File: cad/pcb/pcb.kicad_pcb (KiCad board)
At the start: 4 copper layers, 104 parts, among them X1 USB_C_Receptacle_USB2.0, X2 Bat-Conn, X3 NTC-Conn, X4 SWD-Conn, X5 UART_Conn, Y1 32MHz, Y2 32.768k

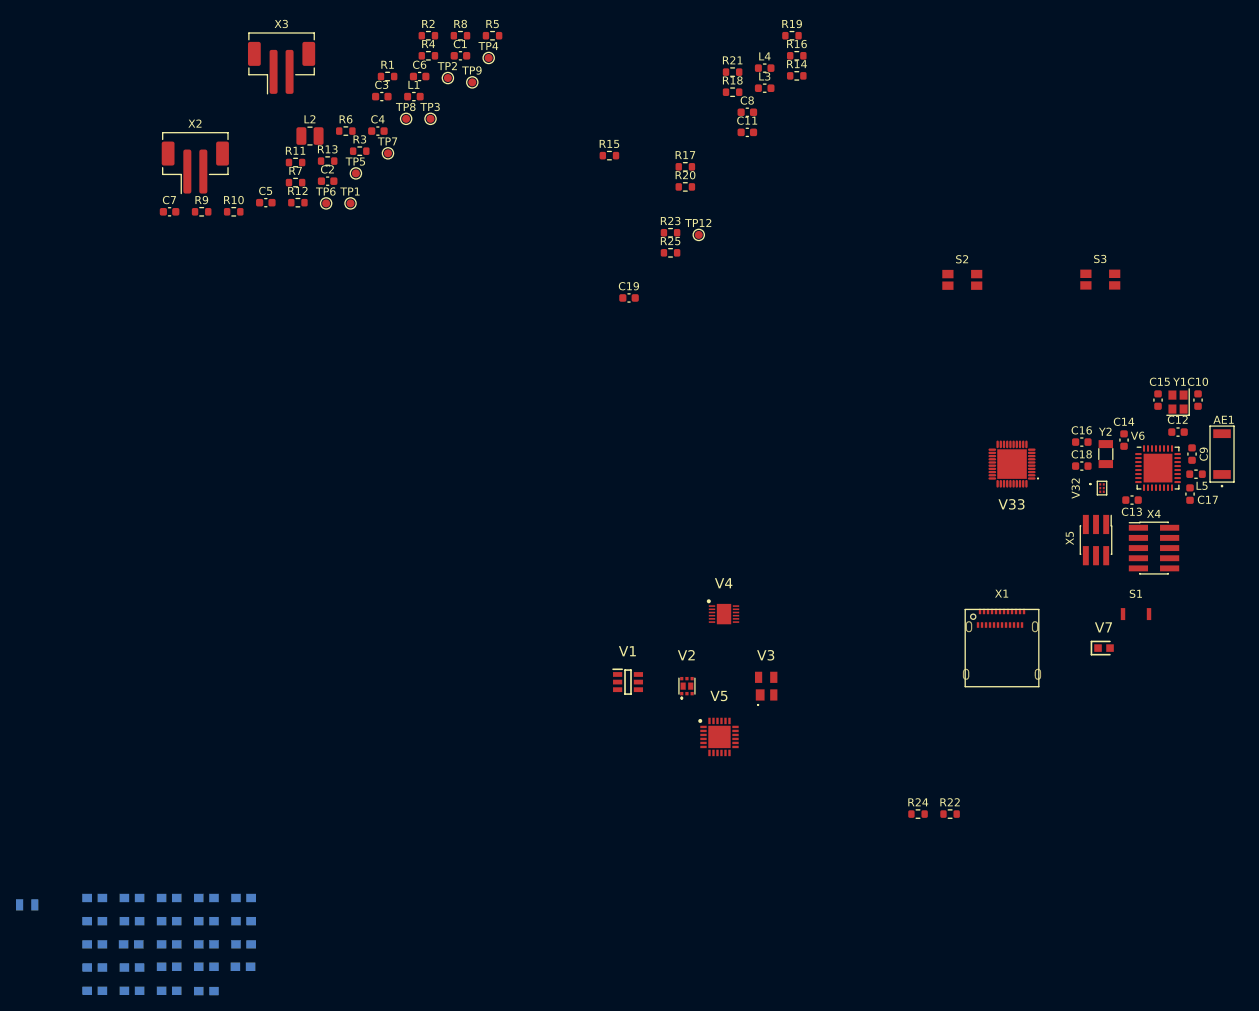
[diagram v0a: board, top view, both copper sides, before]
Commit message: finish mcu section in pcb layout
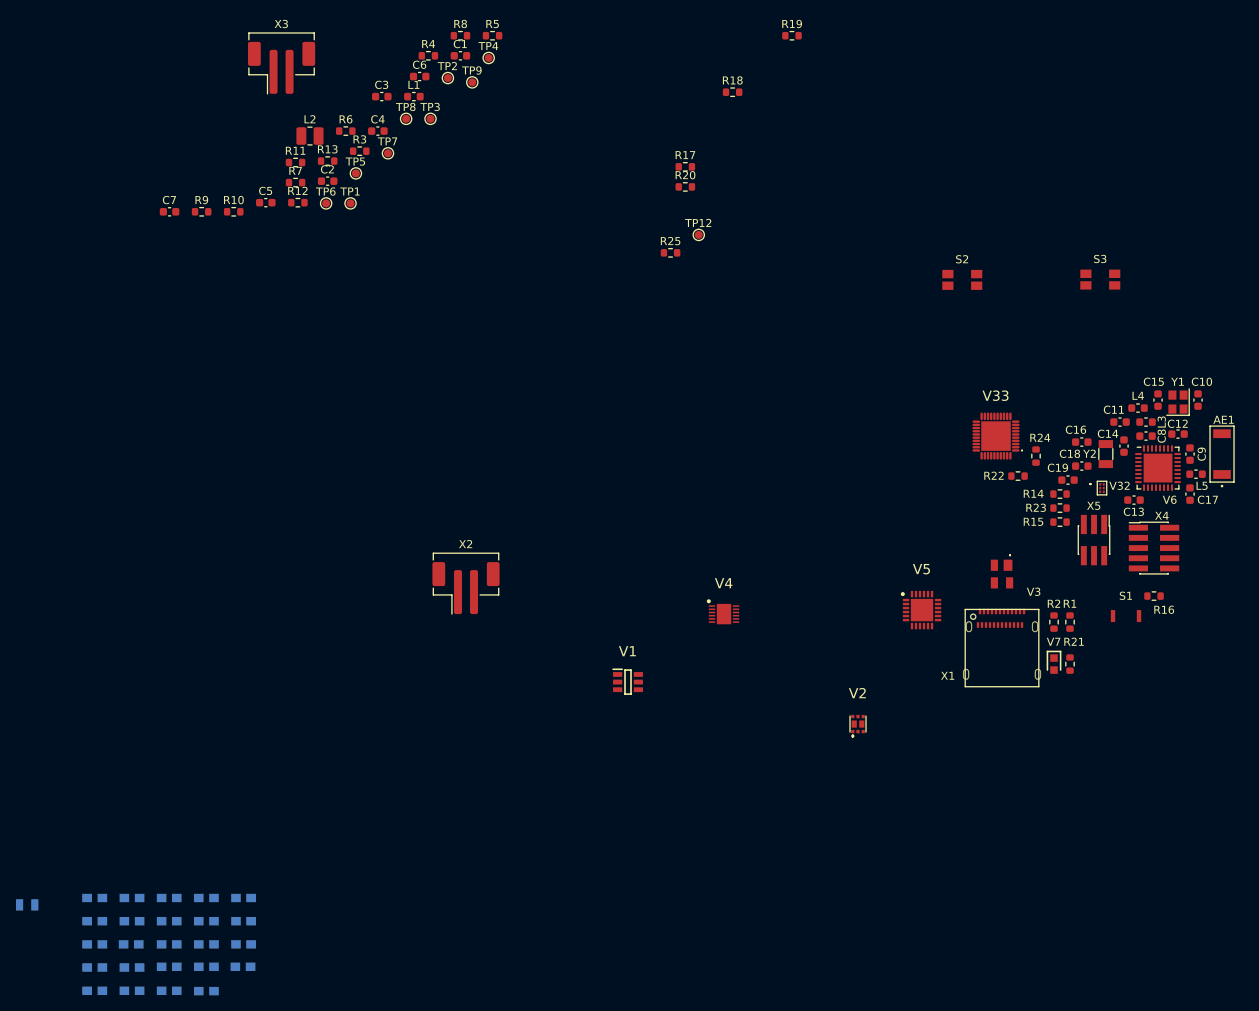
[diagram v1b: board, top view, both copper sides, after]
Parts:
- moved R1 109.2 mm to (158.5, 120.8), turned to 90 degrees
- moved R2 107.2 mm to (156.5, 120.8), turned to 90 degrees
- moved R21 85.2 mm to (158.5, 126.0), turned to -90 degrees
- moved R16 81.0 mm to (169.0, 117.5), turned to 180 degrees
- moved R15 72.6 mm to (157.2, 108.2)
- moved C8 64.2 mm to (168.0, 97.5), turned to 180 degrees
- moved L3 63.4 mm to (168.0, 95.8)
- moved L4 63.1 mm to (167.0, 94.0), turned to 180 degrees
- moved X2 62.5 mm to (83.0, 116.5)
- moved R14 61.8 mm to (157.2, 104.8)
- moved R23 59.6 mm to (157.2, 106.5)
- moved C19 59.4 mm to (158.2, 103.0), turned to 180 degrees
- moved C11 59.0 mm to (164.8, 95.8), turned to 180 degrees
- moved R24 47.1 mm to (154.2, 100.0), turned to -90 degrees
- moved R22 43.1 mm to (152.0, 102.5), turned to 180 degrees
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
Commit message: add power section on pcb layout
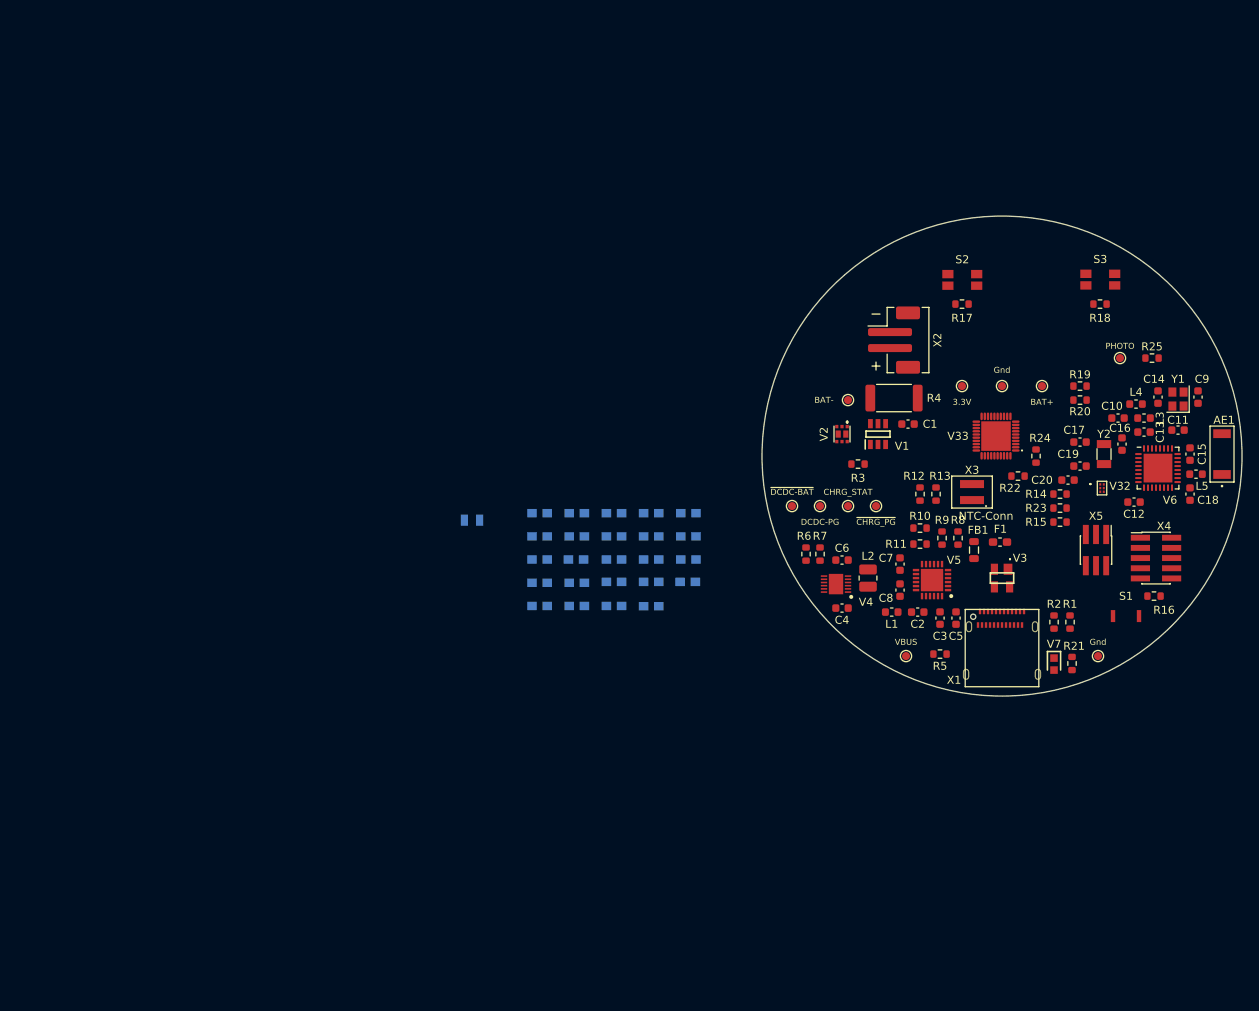
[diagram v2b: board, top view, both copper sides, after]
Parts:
- added C5: 1u, Capacitor_SMD:C_0603_1608Metric, F.Cu at (144.2, 120.2)
- added F1: Fuse_1A, Fuse:Fuse_0603_1608Metric_Pad1.05x0.95mm_HandSolder, F.Cu at (149.8, 110.8)
- added FB1: FerriteBead_Small, Inductor_SMD:L_0805_2012Metric, F.Cu at (146.5, 111.8)
- added TP6: Gnd, TestPoint:TestPoint_Pad_D1.0mm, F.Cu at (162.0, 125.0)
- R4: footprint Resistor_SMD:R_0603_1608Metric -> Resistor_SMD:R_2512_6332Metric
- X3: footprint Connector_JST:JST_PH_B2B-PH-SM4-TB_1x02-1MP_P2.00mm_Vertical -> myLib:PinHeader_P2mm_1x02_SMD
- moved C8 102.8 mm to (137.2, 116.8), turned to -90 degrees
- moved X3 101.3 mm to (146.2, 104.5), turned to 90 degrees
- moved R9 101.1 mm to (142.5, 110.2), turned to -90 degrees
- moved C3 95.5 mm to (142.2, 120.2), turned to -90 degrees
- moved R5 95.4 mm to (142.2, 124.8), turned to 180 degrees
- moved R10 94.5 mm to (139.8, 109.0)
- moved TP5 91.5 mm to (138.0, 125.0)
- moved R11 91.5 mm to (139.8, 111.0)
- moved C2 91.3 mm to (139.5, 119.5), turned to 180 degrees
- moved L2 89.0 mm to (133.2, 115.2), turned to 90 degrees
- moved R8 88.4 mm to (144.5, 110.2), turned to -90 degrees
- moved L1 87.9 mm to (136.2, 119.5), turned to 180 degrees
- moved R13 86.7 mm to (141.8, 104.8), turned to 90 degrees
- moved R12 85.9 mm to (139.8, 104.8), turned to -90 degrees
- moved C7 85.6 mm to (137.2, 113.5), turned to 90 degrees
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- renumbered C11 to C10, C12 to C11, C13 to C12, C8 to C13, C15 to C14, C9 to C15, C14 to C16, C16 to C17, C17 to C18, C18 to C19, C19 to C20, C5 to C6, C6 to C7, C7 to C8, C10 to C9, TP9 to TP10, TP12 to TP11, TP6 to TP7, TP7 to TP8, TP8 to TP9
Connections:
- V3 pad 1: VBUS -> VBUS_CONN
- X1 pad A4: VBUS -> VBUS_CONN
- X1 pad A9: VBUS -> VBUS_CONN
- X1 pad B4: VBUS -> VBUS_CONN
- X1 pad B9: VBUS -> VBUS_CONN
- X2 pad 1: BAT_PROT+ -> BAT-
- X2 pad 2: BAT- -> BAT_PROT+
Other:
- board outline added: 60 x 60 mm

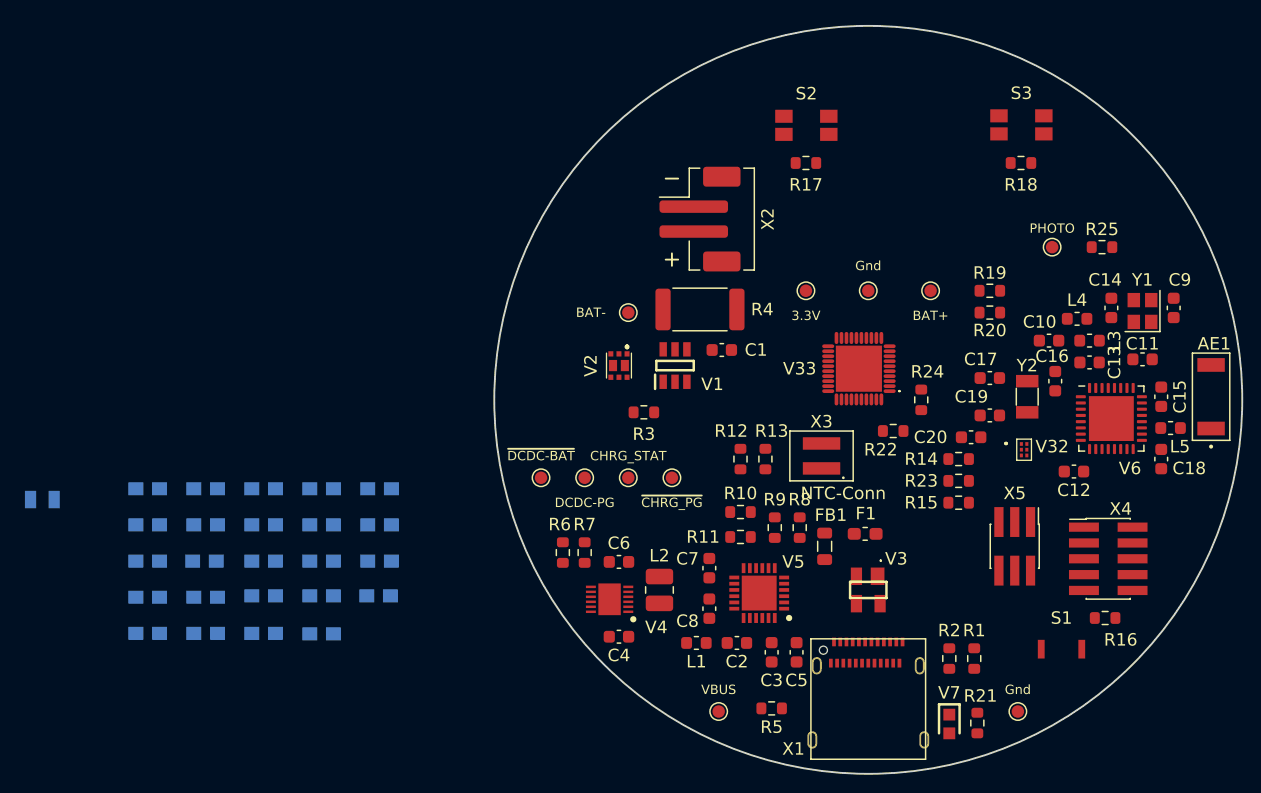
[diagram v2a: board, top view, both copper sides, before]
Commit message: add back layer led-ring
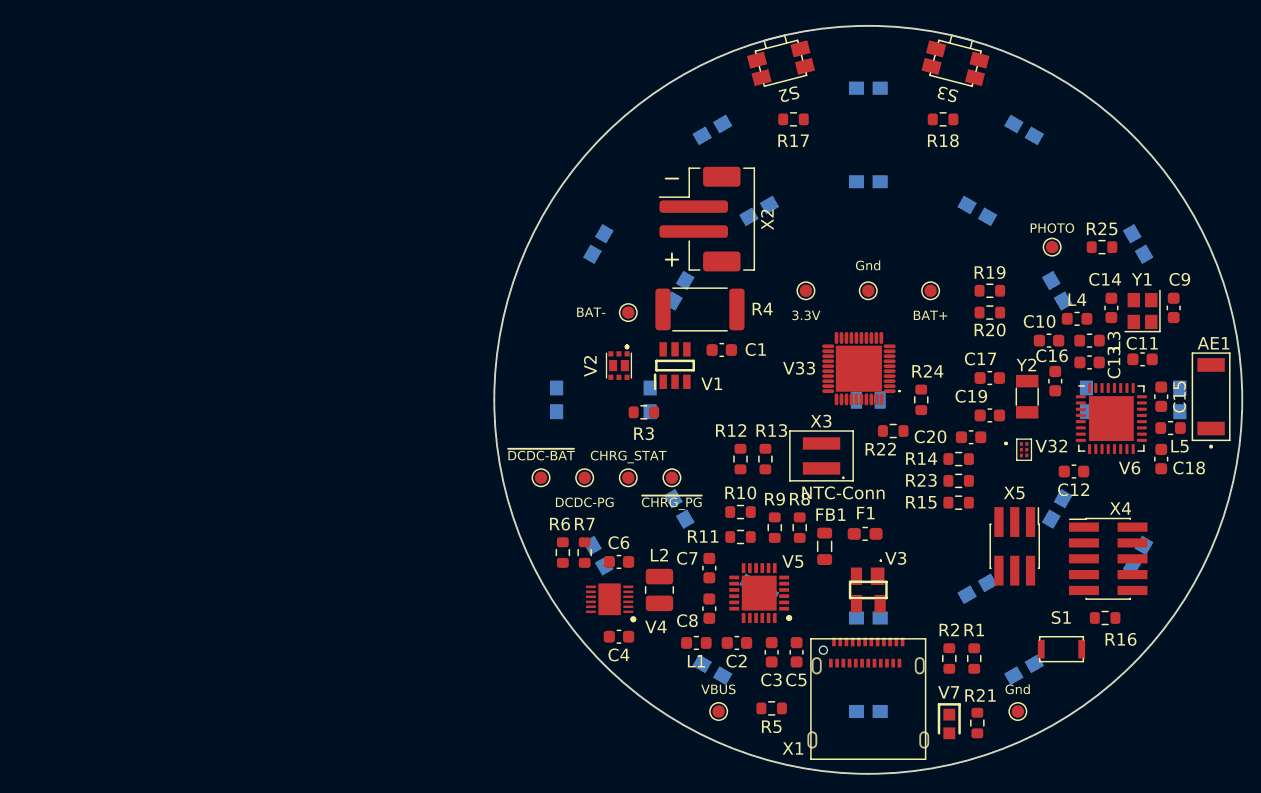
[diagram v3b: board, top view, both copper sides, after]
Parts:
- S2, S3: footprint myLib:Tactile_Panasonic_EVQ-P7J01P -> myLib:Tactile_Panasonic_EVQP7J01P
- moved V18 81.1 mm to (171.7, 87.5), turned to -60 degrees
- moved V16 79.5 mm to (171.7, 112.5), turned to -120 degrees
- moved V19 76.0 mm to (162.5, 78.3), turned to -30 degrees
- moved V29 71.0 mm to (167.5, 100.0), turned to -90 degrees
- moved V17 69.2 mm to (175.0, 100.0), turned to -90 degrees
- moved V34 66.7 mm to (150.0, 100.0), turned to 0 degrees
- moved V30 66.4 mm to (165.2, 91.2), turned to -60 degrees
- moved V20 65.3 mm to (150.0, 82.5), turned to 0 degrees
- moved V31 63.8 mm to (158.8, 84.8), turned to -30 degrees
- moved V8 63.7 mm to (150.0, 75.0), turned to 0 degrees
- moved V28 59.0 mm to (165.2, 108.8), turned to -120 degrees
- moved V27 57.4 mm to (158.8, 115.2), turned to -150 degrees
- moved V21 52.6 mm to (141.2, 84.8), turned to 30 degrees
- moved V15 52.4 mm to (162.5, 121.7), turned to -150 degrees
- moved V9 51.9 mm to (137.5, 78.3), turned to 30 degrees
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
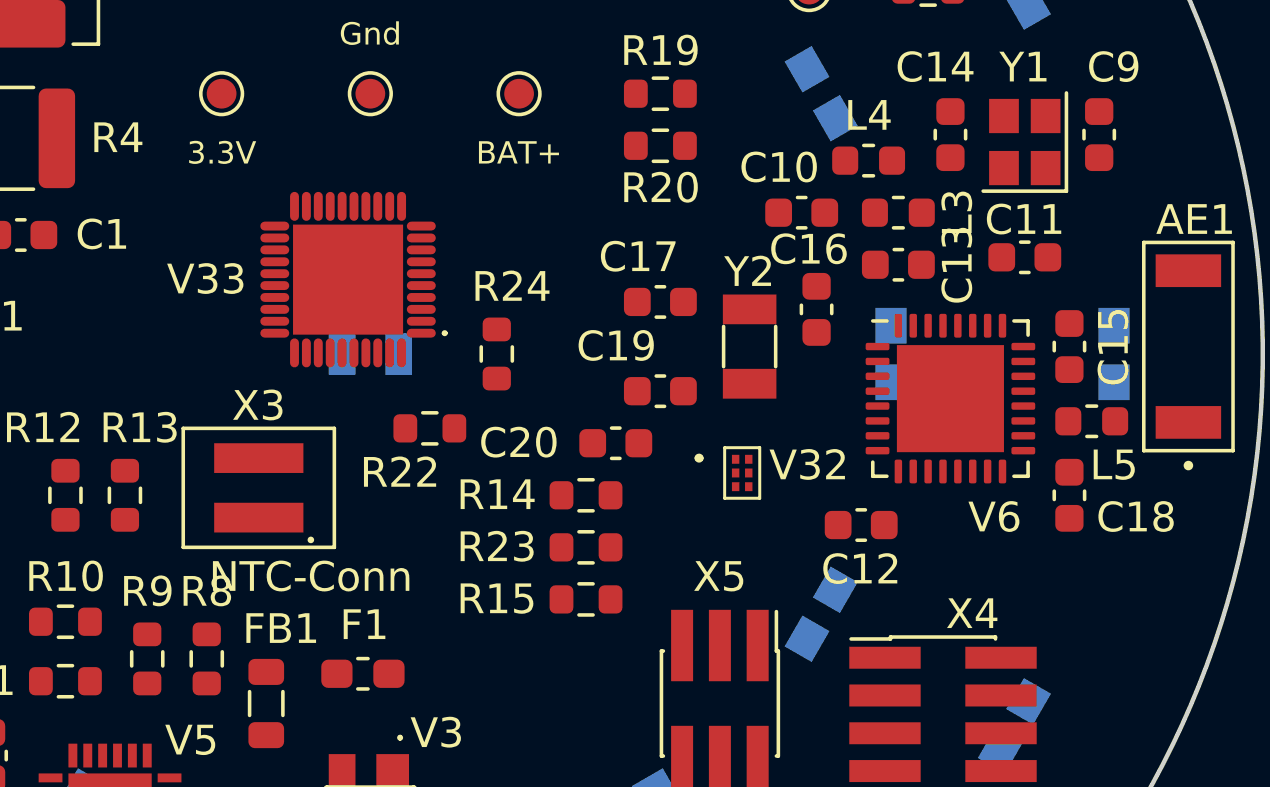
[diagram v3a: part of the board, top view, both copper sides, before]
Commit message: finish back layer placement
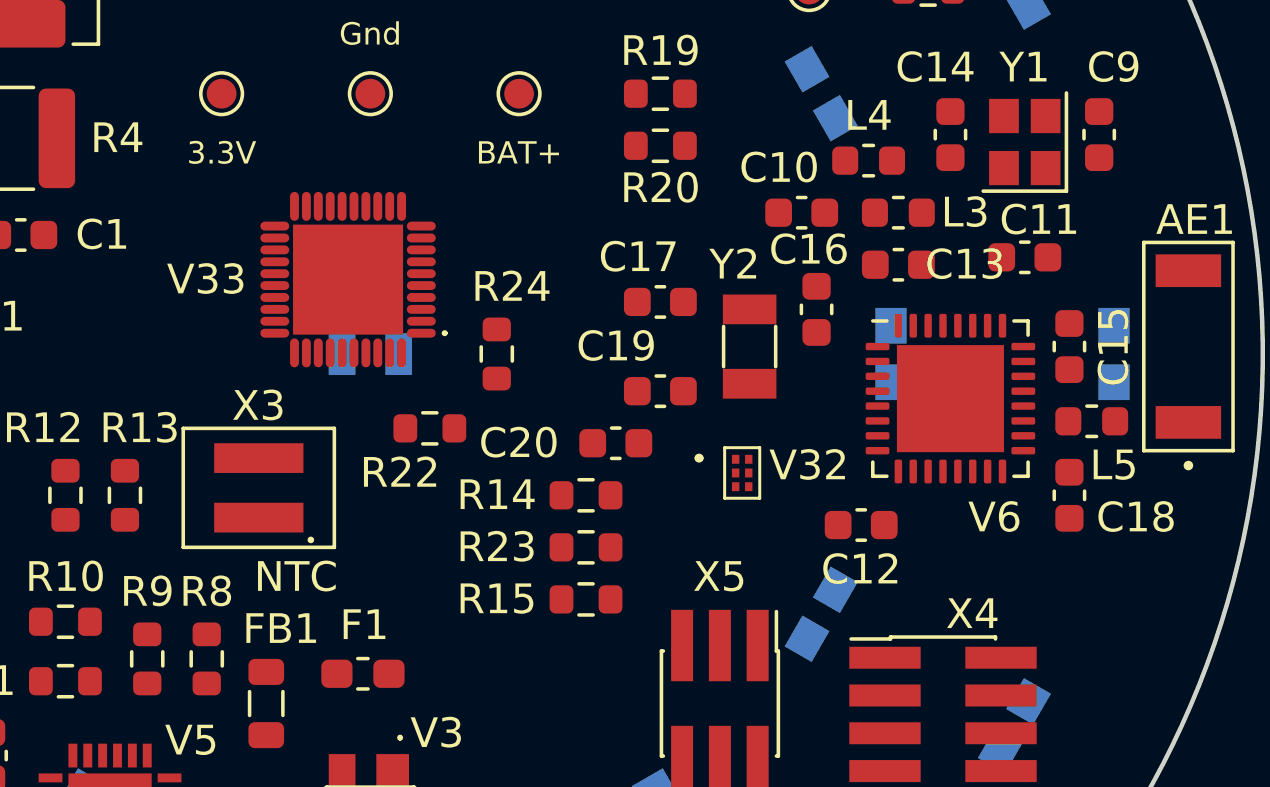
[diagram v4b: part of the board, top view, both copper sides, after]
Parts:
- X3: value NTC-Conn -> NTC
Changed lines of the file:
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@@
     (property "Sheetname" "MCU")
     (attr smd)
-    (fp_text reference "Y2" (at -2.5 0 180) (layer "F.SilkS")
+    (fp_text reference "Y2" (at -2.75 0.5 180) (layer "F.SilkS")
       (effects (font (size 1 1) (thickness 0.15)))
     )
@@
     (property "Sheetname" "MCU")
     (attr smd)
-    (fp_text reference "L3" (at 2 0 90) (layer "F.SilkS")
+    (fp_text reference "L3" (at 2.25 0 180) (layer "F.SilkS")
       (effects (font (size 1 1) (thickness 0.15)))
     )
@@
     (property "Sheetname" "MCU")
     (attr smd)
-    (fp_text reference "C13" (at -2 0 90) (layer "F.SilkS")
+    (fp_text reference "C13" (at -2.25 0 180) (layer "F.SilkS")
       (effects (font (size 1 1) (thickness 0.15)))
     )
@@
       (effects (font (size 1 1) (thickness 0.15)))
     )
-    (fp_text value "NTC-Conn" (at -3 1.75 unlocked) (layer "F.SilkS")
+    (fp_text value "NTC" (at -3 1.25 unlocked) (layer "F.SilkS")
       (effects (font (size 1 1) (thickness 0.15)))
     )
@@
     (property "Sheetname" "MCU")
     (attr smd)
-    (fp_text reference "C11" (at 0 -1.25) (layer "F.SilkS")
+    (fp_text reference "C11" (at 0.5 -1.25) (layer "F.SilkS")
       (effects (font (size 1 1) (thickness 0.15)))
     )
@@
     (property "Sheetname" "LED Ring")
     (attr smd)
-    (fp_text reference "V18" (at 0 2.54 -240) (layer "F.Fab")
+    (fp_text reference "V18" (at 0 2.54 -240) (layer "B.Fab")
       (effects (font (size 1.27 1.27) (thickness 0.254)))
     )
@@
   (gr_circle (center 150 100) (end 167.5 100) (layer "Dwgs.User") (width 0.15) (fill none))
   (gr_line (start 142.5 70) (end 142.5 71) (layer "Dwgs.User") (width 0.15))
-  (gr_line (start 120 130) (end 120 70) (layer "Cmts.User") (width 0.15))
-  (gr_line (start 180 100) (end 120 100) (layer "Cmts.User") (width 0.15))
-  (gr_line (start 180 130) (end 120 70) (layer "Cmts.User") (width 0.15))
-  (gr_line (start 180 130) (end 120 130) (layer "Cmts.User") (width 0.15))
-  (gr_line (start 120 130) (end 180 70) (layer "Cmts.User") (width 0.15))
-  (gr_line (start 120 70) (end 180 70) (layer "Cmts.User") (width 0.15))
   (gr_line (start 150 130) (end 150 70) (layer "Cmts.User") (width 0.15))
-  (gr_line (start 180 70) (end 180 130) (layer "Cmts.User") (width 0.15))
   (gr_circle (center 150 100) (end 180 100) (layer "Edge.Cuts") (width 0.15) (fill none))
   (gr_circle (center 150 100) (end 180 100) (layer "Margin") (width 0.15) (fill none))
